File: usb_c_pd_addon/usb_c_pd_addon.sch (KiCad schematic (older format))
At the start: 16 parts, among them J1 USB-C_Female, J3 Conn_01x05, J4 Conn_01x03, J5 Conn_01x01, U1 FUSB302MPX, U2 TPS2592xx

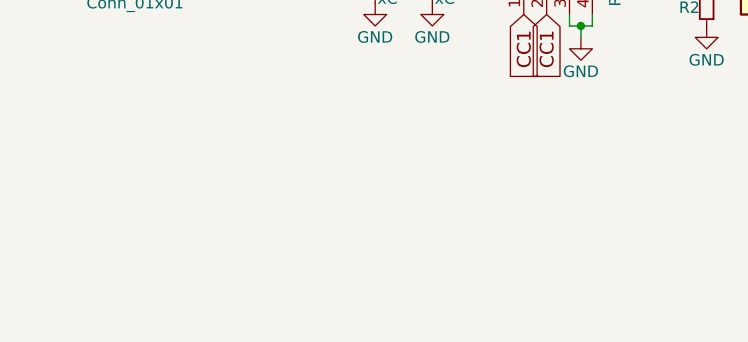
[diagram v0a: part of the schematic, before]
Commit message: USB Type-C mod - v1.0
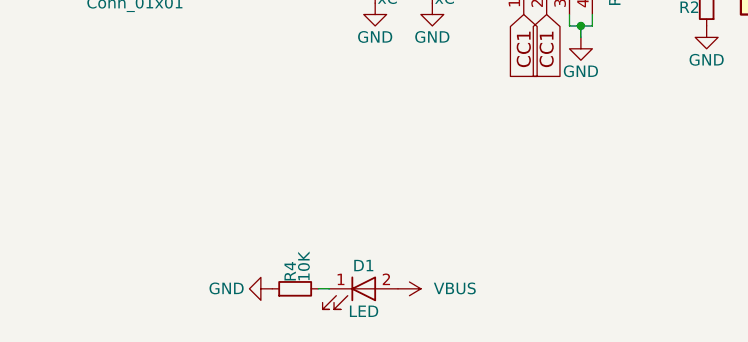
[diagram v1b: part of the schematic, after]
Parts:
- added D1: LED, LEDs:LED_0805_HandSoldering, symbol LED
- added R4: 10K, Resistors_SMD:R_0603_HandSoldering, symbol R_Small
- C2, C3, C4: footprint Capacitors_SMD:C_0603_HandSoldering -> Capacitors_SMD:C_0805_HandSoldering
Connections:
- net GND: now also R4.1
- net VBUS: now also D1.2 (A)
- new net: D1.1 (K), R4.2
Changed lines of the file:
@@
 $EndComp
 $Comp
-L GND #PWR17
+L GND #PWR19
 U 1 1 5BCA61F9
 P 4850 2500
-F 0 "#PWR17" H 4850 2250 50  0001 C CNN
+F 0 "#PWR19" H 4850 2250 50  0001 C CNN
 F 1 "GND" V 4850 2300 50  0000 C CNN
 F 2 "" H 4850 2500 50  0001 C CNN
@@
 $EndComp
 $Comp
-L VBUS #PWR7
+L VBUS #PWR8
 U 1 1 5BCA6353
 P 3750 1800
-F 0 "#PWR7" H 3750 1650 50  0001 C CNN
+F 0 "#PWR8" H 3750 1650 50  0001 C CNN
 F 1 "VBUS" V 3750 2050 50  0000 C CNN
 F 2 "" H 3750 1800 50  0001 C CNN
@@
 $EndComp
 $Comp
-L VBUS #PWR8
+L VBUS #PWR9
 U 1 1 5BCA6396
 P 3750 2300
-F 0 "#PWR8" H 3750 2150 50  0001 C CNN
+F 0 "#PWR9" H 3750 2150 50  0001 C CNN
 F 1 "VBUS" V 3750 2550 50  0000 C CNN
 F 2 "" H 3750 2300 50  0001 C CNN
@@
 $EndComp
 $Comp
-L GND #PWR9
+L GND #PWR10
 U 1 1 5BCA63F2
 P 3750 2600
-F 0 "#PWR9" H 3750 2350 50  0001 C CNN
+F 0 "#PWR10" H 3750 2350 50  0001 C CNN
 F 1 "GND" V 3750 2400 50  0000 C CNN
 F 2 "" H 3750 2600 50  0001 C CNN
@@
 $EndComp
 $Comp
-L GND #PWR6
+L GND #PWR7
 U 1 1 5BCA6409
 P 3750 1500
-F 0 "#PWR6" H 3750 1250 50  0001 C CNN
+F 0 "#PWR7" H 3750 1250 50  0001 C CNN
 F 1 "GND" V 3750 1300 50  0000 C CNN
 F 2 "" H 3750 1500 50  0001 C CNN
@@
 SCL
 $Comp
-L GND #PWR31
+L GND #PWR33
 U 1 1 5BCA64BE
 P 6700 2150
-F 0 "#PWR31" H 6700 1900 50  0001 C CNN
+F 0 "#PWR33" H 6700 1900 50  0001 C CNN
 F 1 "GND" V 6700 1950 50  0000 C CNN
 F 2 "" H 6700 2150 50  0001 C CNN
@@
 $EndComp
 $Comp
-L VCOM #PWR19
+L VCOM #PWR21
 U 1 1 5BCA6420
 P 5000 2000
-F 0 "#PWR19" H 5000 1850 50  0001 C CNN
+F 0 "#PWR21" H 5000 1850 50  0001 C CNN
 F 1 "VCOM" V 5000 2250 50  0000 C CNN
 F 2 "" H 5000 2000 50  0001 C CNN
@@
 $EndComp
 $Comp
-L +3V3 #PWR30
+L +3V3 #PWR32
 U 1 1 5BCA644C
 P 6700 1750
-F 0 "#PWR30" H 6700 1600 50  0001 C CNN
+F 0 "#PWR32" H 6700 1600 50  0001 C CNN
 F 1 "+3V3" H 6700 1890 50  0000 C CNN
 F 2 "" H 6700 1750 50  0001 C CNN
@@
 $EndComp
 $Comp
-L GND #PWR10
+L GND #PWR11
 U 1 1 5BCA646A
 P 3750 2900
-F 0 "#PWR10" H 3750 2650 50  0001 C CNN
+F 0 "#PWR11" H 3750 2650 50  0001 C CNN
 F 1 "GND" V 3750 2700 50  0000 C CNN
 F 2 "" H 3750 2900 50  0001 C CNN
@@
 D+
 $Comp
-L +3V3 #PWR22
+L +3V3 #PWR24
 U 1 1 5BCA6A16
 P 5000 2300
-F 0 "#PWR22" H 5000 2150 50  0001 C CNN
+F 0 "#PWR24" H 5000 2150 50  0001 C CNN
 F 1 "+3V3" V 5000 2550 50  0000 C CNN
 F 2 "" H 5000 2300 50  0001 C CNN
@@
 $EndComp
 $Comp
-L +3V3 #PWR21
+L +3V3 #PWR23
 U 1 1 5BCA6ADF
 P 5000 2200
-F 0 "#PWR21" H 5000 2050 50  0001 C CNN
+F 0 "#PWR23" H 5000 2050 50  0001 C CNN
 F 1 "+3V3" V 5000 2450 50  0000 C CNN
 F 2 "" H 5000 2200 50  0001 C CNN
@@
 INT
 $Comp
-L VCOM #PWR32
+L VCOM #PWR34
 U 1 1 5BCA9760
 P 6700 2450
-F 0 "#PWR32" H 6700 2300 50  0001 C CNN
+F 0 "#PWR34" H 6700 2300 50  0001 C CNN
 F 1 "VCOM" V 6700 2700 50  0000 C CNN
 F 2 "" H 6700 2450 50  0001 C CNN
@@
 NoConn ~ 6700 2550
 $Comp
-L VCOM #PWR20
+L VCOM #PWR22
 U 1 1 5BCA63D6
 P 5000 2100
-F 0 "#PWR20" H 5000 1950 50  0001 C CNN
+F 0 "#PWR22" H 5000 1950 50  0001 C CNN
 F 1 "VCOM" V 5000 2350 50  0000 C CNN
 F 2 "" H 5000 2100 50  0001 C CNN
@@
 CC1
 $Comp
-L GND #PWR16
+L GND #PWR18
 U 1 1 5BCA8CF5
 P 4650 3600
-F 0 "#PWR16" H 4650 3350 50  0001 C CNN
+F 0 "#PWR18" H 4650 3350 50  0001 C CNN
 F 1 "GND" H 4650 3450 50  0000 C CNN
 F 2 "" H 4650 3600 50  0001 C CNN
@@
 $EndComp
 $Comp
-L GND #PWR15
+L GND #PWR17
 U 1 1 5BCA8D19
 P 4450 3000
-F 0 "#PWR15" H 4450 2750 50  0001 C CNN
+F 0 "#PWR17" H 4450 2750 50  0001 C CNN
 F 1 "GND" H 4450 2850 50  0000 C CNN
 F 2 "" H 4450 3000 50  0001 C CNN
@@
 	6400 2650 6700 2650
 $Comp
-L VBUS #PWR25
+L VBUS #PWR27
 U 1 1 5BCA92C4
 P 5650 3000
-F 0 "#PWR25" H 5650 2850 50  0001 C CNN
+F 0 "#PWR27" H 5650 2850 50  0001 C CNN
 F 1 "VBUS" H 5650 3150 50  0000 C CNN
 F 2 "" H 5650 3000 50  0001 C CNN
@@
 Connection ~ 5200 3300
 $Comp
-L GND #PWR26
+L GND #PWR28
 U 1 1 5BCA9428
 P 5650 3600
-F 0 "#PWR26" H 5650 3350 50  0001 C CNN
+F 0 "#PWR28" H 5650 3350 50  0001 C CNN
 F 1 "GND" H 5650 3450 50  0000 C CNN
 F 2 "" H 5650 3600 50  0001 C CNN
@@
 $EndComp
 $Comp
-L GND #PWR24
+L GND #PWR26
 U 1 1 5BCA9451
 P 5200 3550
-F 0 "#PWR24" H 5200 3300 50  0001 C CNN
+F 0 "#PWR26" H 5200 3300 50  0001 C CNN
 F 1 "GND" H 5200 3400 50  0000 C CNN
 F 2 "" H 5200 3550 50  0001 C CNN
@@
 $EndComp
 $Comp
-L VBUS #PWR23
+L VBUS #PWR25
 U 1 1 5BCA947A
 P 5200 3050
-F 0 "#PWR23" H 5200 2900 50  0001 C CNN
+F 0 "#PWR25" H 5200 2900 50  0001 C CNN
 F 1 "VBUS" H 5200 3200 50  0000 C CNN
 F 2 "" H 5200 3050 50  0001 C CNN
@@
 $EndComp
 $Comp
-L GND #PWR27
+L GND #PWR29
 U 1 1 5BCA94E7
 P 6050 3600
-F 0 "#PWR27" H 6050 3350 50  0001 C CNN
+F 0 "#PWR29" H 6050 3350 50  0001 C CNN
 F 1 "GND" H 6050 3450 50  0000 C CNN
 F 2 "" H 6050 3600 50  0001 C CNN
@@
 $EndComp
 $Comp
-L GND #PWR28
+L GND #PWR30
 U 1 1 5BCA95B6
 P 6300 3600
-F 0 "#PWR28" H 6300 3350 50  0001 C CNN
+F 0 "#PWR30" H 6300 3350 50  0001 C CNN
 F 1 "GND" H 6300 3450 50  0000 C CNN
 F 2 "" H 6300 3600 50  0001 C CNN
@@
 	4950 1900 5000 1900
 $Comp
-L VBUS #PWR18
+L VBUS #PWR20
 U 1 1 5BCA62C9
 P 4950 1850
-F 0 "#PWR18" H 4950 1700 50  0001 C CNN
+F 0 "#PWR20" H 4950 1700 50  0001 C CNN
 F 1 "VBUS" H 4950 2000 50  0000 C CNN
 F 2 "" H 4950 1850 50  0001 C CNN
@@
 F 0 "C3" H 4010 3420 50  0000 L CNN
 F 1 "xC" H 4010 3270 50  0000 L CNN
-F 2 "Capacitors_SMD:C_0603_HandSoldering" H 4000 3350 50  0001 C CNN
+F 2 "Capacitors_SMD:C_0805_HandSoldering" H 4000 3350 50  0001 C CNN
 F 3 "" H 4000 3350 50  0001 C CNN
 	1    4000 3350
@@
 $EndComp
 $Comp
-L GND #PWR14
+L GND #PWR16
 U 1 1 5BCA996F
 P 4000 3450
-F 0 "#PWR14" H 4000 3200 50  0001 C CNN
+F 0 "#PWR16" H 4000 3200 50  0001 C CNN
 F 1 "GND" H 4000 3300 50  0000 C CNN
 F 2 "" H 4000 3450 50  0001 C CNN
@@
 $EndComp
 $Comp
-L VBUS #PWR13
+L VBUS #PWR15
 U 1 1 5BCA99A4
 P 4000 3250
-F 0 "#PWR13" H 4000 3100 50  0001 C CNN
+F 0 "#PWR15" H 4000 3100 50  0001 C CNN
 F 1 "VBUS" H 4000 3400 50  0000 C CNN
 F 2 "" H 4000 3250 50  0001 C CNN
@@
 F 0 "C4" H 6560 3420 50  0000 L CNN
 F 1 "xC" H 6560 3270 50  0000 L CNN
-F 2 "Capacitors_SMD:C_0603_HandSoldering" H 6550 3350 50  0001 C CNN
+F 2 "Capacitors_SMD:C_0805_HandSoldering" H 6550 3350 50  0001 C CNN
 F 3 "" H 6550 3350 50  0001 C CNN
 	1    6550 3350
@@
 $EndComp
 $Comp
-L GND #PWR29
+L GND #PWR31
 U 1 1 5BCA9A9C
 P 6550 3450
-F 0 "#PWR29" H 6550 3200 50  0001 C CNN
+F 0 "#PWR31" H 6550 3200 50  0001 C CNN
 F 1 "GND" H 6550 3300 50  0000 C CNN
 F 2 "" H 6550 3450 50  0001 C CNN
@@
 F 0 "C2" H 3760 3420 50  0000 L CNN
 F 1 "xC" H 3760 3270 50  0000 L CNN
-F 2 "Capacitors_SMD:C_0603_HandSoldering" H 3750 3350 50  0001 C CNN
+F 2 "Capacitors_SMD:C_0805_HandSoldering" H 3750 3350 50  0001 C CNN
 F 3 "" H 3750 3350 50  0001 C CNN
 	1    3750 3350
@@
 $EndComp
 $Comp
-L GND #PWR12
+L GND #PWR13
 U 1 1 5BCA9B36
 P 3750 3450
-F 0 "#PWR12" H 3750 3200 50  0001 C CNN
+F 0 "#PWR13" H 3750 3200 50  0001 C CNN
 F 1 "GND" H 3750 3300 50  0000 C CNN
 F 2 "" H 3750 3450 50  0001 C CNN
@@
 $EndComp
 $Comp
-L VBUS #PWR11
+L VBUS #PWR12
 U 1 1 5BCA9B3C
 P 3750 3250
-F 0 "#PWR11" H 3750 3100 50  0001 C CNN
+F 0 "#PWR12" H 3750 3100 50  0001 C CNN
 F 1 "VBUS" H 3750 3400 50  0000 C CNN
 F 2 "" H 3750 3250 50  0001 C CNN
@@
 	1    0    0    -1
 $EndComp
+$Comp
+L LED D1
+U 1 1 5BCAB771
+P 3700 4700
+F 0 "D1" H 3700 4800 50  0000 C CNN
+F 1 "LED" H 3700 4600 50  0000 C CNN
+F 2 "LEDs:LED_0805_HandSoldering" H 3700 4700 50  0001 C CNN
+F 3 "" H 3700 4700 50  0001 C CNN
+	1    3700 4700
+	1    0    0    -1
+$EndComp
+$Comp
+L R_Small R4
+U 1 1 5BCAB7D3
+P 3400 4700
+F 0 "R4" H 3430 4720 50  0000 L CNN
+F 1 "10K" H 3430 4660 50  0000 L CNN
+F 2 "Resistors_SMD:R_0603_HandSoldering" H 3400 4700 50  0001 C CNN
+F 3 "" H 3400 4700 50  0001 C CNN
+	1    3400 4700
+	0    -1   -1   0
+$EndComp
+Wire Wire Line
+	3500 4700 3550 4700
+$Comp
+L GND #PWR6
+U 1 1 5BCAB945
+P 3300 4700
+F 0 "#PWR6" H 3300 4450 50  0001 C CNN
+F 1 "GND" V 3300 4500 50  0000 C CNN
+F 2 "" H 3300 4700 50  0001 C CNN
+F 3 "" H 3300 4700 50  0001 C CNN
+	1    3300 4700
+	0    1    1    0
+$EndComp
+$Comp
+L VBUS #PWR14
+U 1 1 5BCAB998
+P 3850 4700
+F 0 "#PWR14" H 3850 4550 50  0001 C CNN
+F 1 "VBUS" V 3850 4950 50  0000 C CNN
+F 2 "" H 3850 4700 50  0001 C CNN
+F 3 "" H 3850 4700 50  0001 C CNN
+	1    3850 4700
+	0    1    1    0
+$EndComp
 $EndSCHEMATC
